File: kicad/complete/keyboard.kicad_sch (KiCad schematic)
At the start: 74 parts, among them P2 KEYB CONN 1

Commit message: erc and llm review complete
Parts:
- R16: renamed from R12; value R_Small_US -> 330R
- renumbered D9 to D10, D10 to D11, D11 to D12, D12 to D13, D13 to D14, D14 to D15, D15 to D16, D16 to D17, D17 to D18, D18 to D19, D19 to D20, D20 to D21, D21 to D22, D22 to D23, D23 to D24, D24 to D25, D25 to D26, D26 to D27, D27 to D28, D28 to D29, D2 to D3, D29 to D30, D68 to D31, D69 to D32, D30 to D33, D31 to D34, D32 to D35, D33 to D36, D1 to D37, D3 to D4, D4 to D5, D5 to D6, D6 to D7, D7 to D8, D8 to D9, MX40 to MX30, MX41 to MX31, MX30 to MX32, MX31 to MX33, MX32 to MX34, MX33 to MX35, R11 to R15

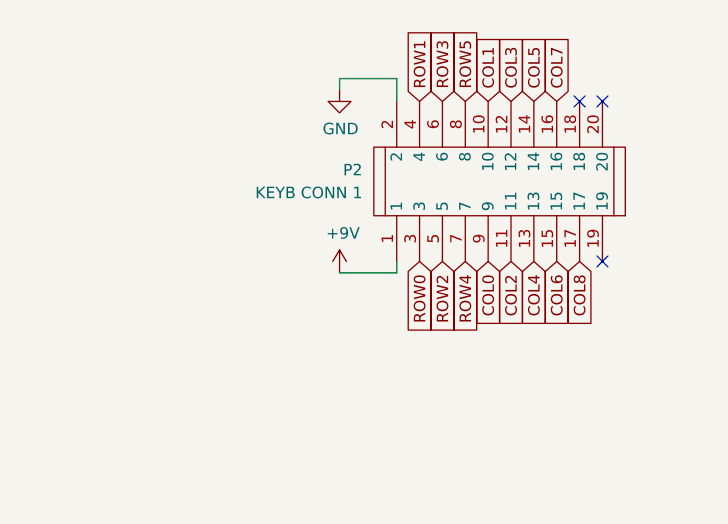
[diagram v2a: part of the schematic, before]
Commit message: updated keyboard connector pinout for better trace routing (hopefully)
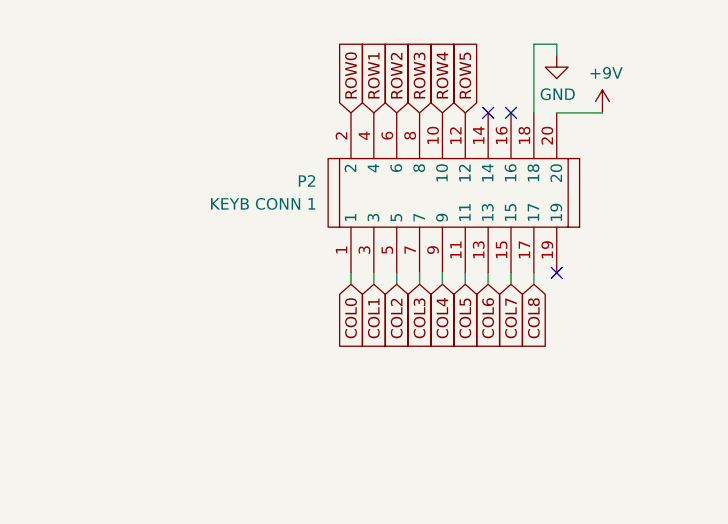
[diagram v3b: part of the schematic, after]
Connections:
- net +9V: now also P2.20; no longer P2.1
- net COL0: now also P2.1; no longer P2.9
- net COL1: now also P2.3; no longer P2.10
- net COL2: now also P2.5; no longer P2.11
- net COL3: now also P2.7; no longer P2.12
- net COL4: now also P2.9; no longer P2.13
- net COL5: now also P2.11; no longer P2.14
- net COL6: now also P2.13; no longer P2.15
- net COL7: now also P2.15; no longer P2.16
- net GND: now also P2.18; no longer P2.2
- net ROW0: now also P2.2; no longer P2.3
- net ROW2: now also P2.6; no longer P2.5
- net ROW3: now also P2.8; no longer P2.6
- net ROW4: now also P2.10; no longer P2.7
- net ROW5: now also P2.12; no longer P2.8
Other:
- moved on the sheet: P2

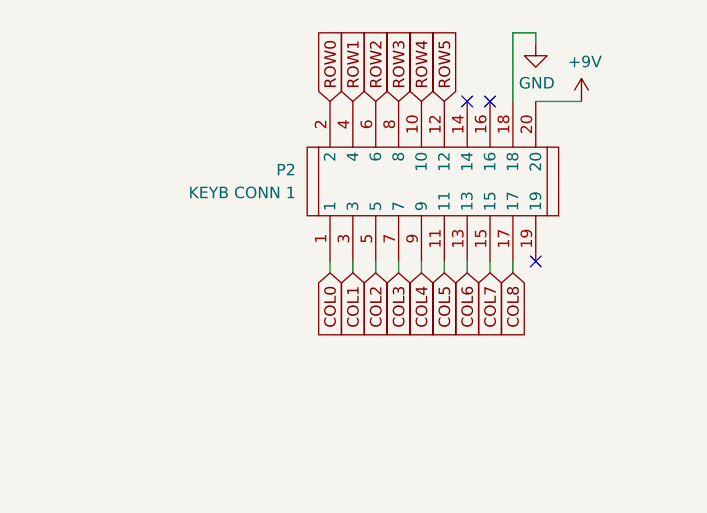
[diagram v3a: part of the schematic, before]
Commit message: updated keyboard connector pinout again for better routing
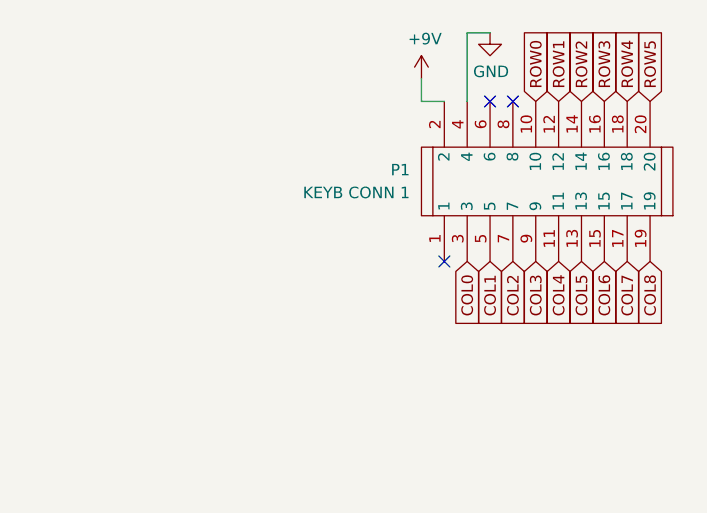
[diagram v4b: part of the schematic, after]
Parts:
- removed P2: KEYB CONN 1, EasyEDA_Lib:IDC-TH_20P-L33.0-W13.8-H-M-R2-C10-P2.54-S2.54-TR, symbol EasyEDA_Lib:IDC Box 2X10 2.54MM
- added P1: KEYB CONN 1, EasyEDA_Lib:IDC-TH_20P-L33.0-W13.8-H-M-R2-C10-P2.54-S2.54-TR, symbol EasyEDA_Lib:IDC Box 2X10 2.54MM
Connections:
- net +9V: now also P1.2
- net COL0: now also P1.3
- net COL1: now also P1.5
- net COL2: now also P1.7
- net COL3: now also P1.9
- net COL4: now also P1.11
- net COL5: now also P1.13
- net COL6: now also P1.15
- net COL7: now also P1.17
- net COL8: now also P1.19
- net GND: now also P1.4
- net ROW0: now also P1.10
- net ROW1: now also P1.12
- net ROW2: now also P1.14
- net ROW3: now also P1.16
- net ROW4: now also P1.18
- net ROW5: now also P1.20
